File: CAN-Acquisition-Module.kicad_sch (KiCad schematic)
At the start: 0 parts

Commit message: Finished CAN section
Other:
- sheet CANbus ports: added CAN_PIN5, CAN_PIN8; removed none
- sheet MCU ports: added CAN_PIN5, CAN_PIN8; removed none
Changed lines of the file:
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@@
 (kicad_sch (version 20211123) (generator eeschema)
   (paper "A4")
-  (wire (pts (xy 88.9 46.99) (xy 73.66 46.99))
+  (wire (pts (xy 123.19 67.31) (xy 99.06 67.31))
     (stroke (width 0) (type default) (color 0 0 0 0))
   )
@@
     (stroke (width 0) (type default) (color 0 0 0 0))
   )
+  (wire (pts (xy 101.6 69.85) (xy 101.6 107.95))
+    (stroke (width 0) (type default) (color 0 0 0 0))
+  )
   (wire (pts (xy 123.19 60.96) (xy 91.44 60.96))
     (stroke (width 0) (type default) (color 0 0 0 0))
@@
     (stroke (width 0) (type default) (color 0 0 0 0))
   )
+  (wire (pts (xy 99.06 105.41) (xy 73.66 105.41))
+    (stroke (width 0) (type default) (color 0 0 0 0))
+  )
+  (wire (pts (xy 123.19 69.85) (xy 101.6 69.85))
+    (stroke (width 0) (type default) (color 0 0 0 0))
+  )
+  (wire (pts (xy 99.06 67.31) (xy 99.06 105.41))
+    (stroke (width 0) (type default) (color 0 0 0 0))
+  )
   (wire (pts (xy 91.44 60.96) (xy 91.44 99.06))
     (stroke (width 0) (type default) (color 0 0 0 0))
   )
-  (wire (pts (xy 88.9 34.29) (xy 88.9 46.99))
-    (stroke (width 0) (type default) (color 0 0 0 0))
-  )
   (wire (pts (xy 153.67 31.75) (xy 153.67 43.18))
     (stroke (width 0) (type default) (color 0 0 0 0))
   )
-  (wire (pts (xy 43.18 52.07) (xy 39.37 52.07))
+  (wire (pts (xy 41.91 39.37) (xy 39.37 39.37))
+    (stroke (width 0) (type default) (color 0 0 0 0))
+  )
+  (wire (pts (xy 101.6 107.95) (xy 73.66 107.95))
     (stroke (width 0) (type default) (color 0 0 0 0))
   )
@@
     (stroke (width 0) (type default) (color 0 0 0 0))
   )
-  (wire (pts (xy 39.37 52.07) (xy 39.37 101.6))
-    (stroke (width 0) (type default) (color 0 0 0 0))
-  )
-  (wire (pts (xy 140.97 34.29) (xy 88.9 34.29))
+  (wire (pts (xy 39.37 39.37) (xy 39.37 101.6))
+    (stroke (width 0) (type default) (color 0 0 0 0))
+  )
+  (wire (pts (xy 72.39 34.29) (xy 140.97 34.29))
     (stroke (width 0) (type default) (color 0 0 0 0))
   )
@@
       (effects (font (size 1.27 1.27)) (justify right))
     )
-    (pin "CAN_TX" input (at 123.19 60.96 180)
-      (effects (font (size 1.27 1.27)) (justify left))
-    )
     (pin "CAN_RX" input (at 123.19 63.5 180)
       (effects (font (size 1.27 1.27)) (justify left))
     )
-  )
-  (sheet (at 43.18 43.18) (size 30.48 24.13) (fields_autoplaced)
+    (pin "CAN_PIN8" output (at 123.19 67.31 180)
+      (effects (font (size 1.27 1.27)) (justify left))
+    )
+    (pin "CAN_PIN5" output (at 123.19 69.85 180)
+      (effects (font (size 1.27 1.27)) (justify left))
+    )
+    (pin "CAN_TX" output (at 123.19 60.96 180)
+      (effects (font (size 1.27 1.27)) (justify left))
+    )
+  )
+  (sheet (at 41.91 30.48) (size 30.48 24.13) (fields_autoplaced)
     (stroke (width 0) (type solid) (color 0 0 0 0))
     (fill (color 0 0 0 0.0000))
-    (property "Sheet name" "Power" (id 0) (at 43.18 42.4684 0)
+    (property "Sheet name" "Power" (id 0) (at 41.91 29.7684 0)
       (effects (font (size 1.27 1.27)) (justify left bottom))
     )
-    (property "Sheet file" "CAN-Acquisition-Module_Power.kicad_sch" (id 1) (at 43.18 67.8946 0)
+    (property "Sheet file" "CAN-Acquisition-Module_Power.kicad_sch" (id 1) (at 41.91 55.1946 0)
       (effects (font (size 1.27 1.27)) (justify left top))
     )
-    (pin "V_CAN" input (at 43.18 52.07 180)
-      (effects (font (size 1.27 1.27)) (justify left))
-    )
-    (pin "V_USB" input (at 73.66 46.99 0)
+    (pin "V_CAN" input (at 41.91 39.37 180)
+      (effects (font (size 1.27 1.27)) (justify left))
+    )
+    (pin "V_USB" input (at 72.39 34.29 0)
       (effects (font (size 1.27 1.27)) (justify right))
     )
@@
       (effects (font (size 1.27 1.27)) (justify right))
     )
-    (pin "CAN_RX" input (at 73.66 101.6 0)
+    (pin "CAN_PIN8" input (at 73.66 105.41 0)
+      (effects (font (size 1.27 1.27)) (justify right))
+    )
+    (pin "CAN_PIN5" input (at 73.66 107.95 0)
+      (effects (font (size 1.27 1.27)) (justify right))
+    )
+    (pin "CAN_RX" output (at 73.66 101.6 0)
       (effects (font (size 1.27 1.27)) (justify right))
     )
@@
       (reference "#PWR?") (unit 1) (value "GND") (footprint "")
     )
+    (path "/6a23b5b9-2864-4994-bd7a-8563b9182093/14ab098c-cdf6-4c2b-873a-413a652c8ff3"
+      (reference "#PWR?") (unit 1) (value "+3.3V") (footprint "")
+    )
     (path "/00000000-0000-0000-0000-0000628fba98/1a6c513b-8826-4fc6-be8a-b124c5226464"
       (reference "#PWR?") (unit 1) (value "GND") (footprint "")
@@
     )
     (path "/6a23b5b9-2864-4994-bd7a-8563b9182093/2430da88-04ae-4554-86f4-b38352234578"
+      (reference "#PWR?") (unit 1) (value "GND") (footprint "")
+    )
+    (path "/6a23b5b9-2864-4994-bd7a-8563b9182093/2fbbc203-31f8-4993-bf01-97a3d719ff97"
       (reference "#PWR?") (unit 1) (value "GND") (footprint "")
     )
@@
       (reference "#PWR?") (unit 1) (value "GND") (footprint "")
     )
+    (path "/6a23b5b9-2864-4994-bd7a-8563b9182093/be75ac2c-6454-4f5d-8edd-4ad70bd6276d"
+      (reference "#PWR?") (unit 1) (value "GND") (footprint "")
+    )
     (path "/6a23b5b9-2864-4994-bd7a-8563b9182093/d32dccac-ba40-4b97-a43f-d2ceaf85d73f"
       (reference "#PWR?") (unit 1) (value "GND") (footprint "")
@@
       (reference "#PWR?") (unit 1) (value "+3.3V") (footprint "")
     )
+    (path "/6a23b5b9-2864-4994-bd7a-8563b9182093/dda03ce5-e120-46e0-8597-3a35c9a772e6"
+      (reference "#PWR?") (unit 1) (value "+3.3V") (footprint "")
+    )
     (path "/00000000-0000-0000-0000-0000628fba98/ddedcedf-4555-4d19-bad5-e9dd0770639d"
       (reference "#PWR?") (unit 1) (value "GND") (footprint "")
     )
+    (path "/6a23b5b9-2864-4994-bd7a-8563b9182093/e70d5354-397b-4ea4-a225-d4fa715af3bd"
+      (reference "#PWR?") (unit 1) (value "GND") (footprint "")
+    )
     (path "/6a23b5b9-2864-4994-bd7a-8563b9182093/edd17358-9720-40f3-bb9c-b039179ec970"
       (reference "#PWR?") (unit 1) (value "GND") (footprint "")
@@
     )
     (path "/2306ed72-7073-467c-a255-2365c3b83f36/faa4a203-2c3e-4e45-87a6-ff0eb6a4b99f"
+      (reference "#PWR?") (unit 1) (value "GND") (footprint "")
+    )
+    (path "/6a23b5b9-2864-4994-bd7a-8563b9182093/fb2e8c3c-f406-41c1-92ba-9511cdd26a4d"
       (reference "#PWR?") (unit 1) (value "GND") (footprint "")
     )
@@
       (reference "C?") (unit 1) (value "1 uF") (footprint "Capacitor_SMD:C_0603_1608Metric")
     )
+    (path "/6a23b5b9-2864-4994-bd7a-8563b9182093/82a72df0-9101-40a1-a39e-495f466dd76d"
+      (reference "C?") (unit 1) (value "F") (footprint "Capacitor_SMD:C_0603_1608Metric")
+    )
+    (path "/6a23b5b9-2864-4994-bd7a-8563b9182093/9b59bb94-5ec5-41d6-a90a-50c77b045610"
+      (reference "C?") (unit 1) (value "F") (footprint "Capacitor_SMD:C_0603_1608Metric")
+    )
     (path "/6a23b5b9-2864-4994-bd7a-8563b9182093/a57b452e-51f4-4a6f-81d8-6d70dc434fc1"
       (reference "C?") (unit 1) (value "47 pF") (footprint "Capacitor_SMD:C_0603_1608Metric")
@@
       (reference "R?") (unit 1) (value "100 Ω") (footprint "Resistor_SMD:R_0805_2012Metric")
     )
+    (path "/6a23b5b9-2864-4994-bd7a-8563b9182093/0c6df487-3e31-43d7-bd79-da39a42b0f83"
+      (reference "R?") (unit 1) (value "Ω") (footprint "Resistor_SMD:R_0603_1608Metric")
+    )
+    (path "/6a23b5b9-2864-4994-bd7a-8563b9182093/1199abe3-116f-474b-9e98-49648be6ba96"
+      (reference "R?") (unit 1) (value " Ω") (footprint "Resistor_SMD:R_0603_1608Metric")
+    )
+    (path "/6a23b5b9-2864-4994-bd7a-8563b9182093/1cf81b43-2c10-41da-9491-13a80c1363a9"
+      (reference "R?") (unit 1) (value " Ω") (footprint "Resistor_SMD:R_0603_1608Metric")
+    )
     (path "/6a23b5b9-2864-4994-bd7a-8563b9182093/30955db8-291f-483c-8e4c-3c1d0d742d2b"
       (reference "R?") (unit 1) (value "59Ω-62Ω") (footprint "Resistor_SMD:R_1206_3216Metric")
@@
       (reference "R?") (unit 1) (value "27 Ω") (footprint "Resistor_SMD:R_0603_1608Metric")
     )
+    (path "/6a23b5b9-2864-4994-bd7a-8563b9182093/62f65d79-a6a8-40d5-8263-0bce308bb147"
+      (reference "R?") (unit 1) (value "1 kΩ") (footprint "Resistor_SMD:R_0603_1608Metric")
+    )
     (path "/2306ed72-7073-467c-a255-2365c3b83f36/a907d3ec-4367-4ba0-821c-bcd0f98d1cbc"
       (reference "R?") (unit 1) (value "10 kΩ") (footprint "Resistor_SMD:R_0603_1608Metric")
@@
       (reference "R?") (unit 1) (value "47 kΩ") (footprint "Resistor_SMD:R_0603_1608Metric")
     )
+    (path "/6a23b5b9-2864-4994-bd7a-8563b9182093/e90c2505-6430-498e-9243-2604403d18d0"
+      (reference "R?") (unit 1) (value " Ω") (footprint "Resistor_SMD:R_0603_1608Metric")
+    )
     (path "/2306ed72-7073-467c-a255-2365c3b83f36/ec01bf59-6fcb-4ded-ba21-75edfeff7f43"
       (reference "R?") (unit 1) (value "27 Ω") (footprint "Resistor_SMD:R_0603_1608Metric")
     )
+    (path "/6a23b5b9-2864-4994-bd7a-8563b9182093/ef53684a-960f-4291-abcd-f8fe274048cb"
+      (reference "R?") (unit 1) (value "Ω") (footprint "Resistor_SMD:R_0603_1608Metric")
+    )
+    (path "/6a23b5b9-2864-4994-bd7a-8563b9182093/f4e8f079-13e2-474d-b2a5-b77899afb5ca"
+      (reference "R?") (unit 1) (value "22 kΩ") (footprint "Resistor_SMD:R_0603_1608Metric")
+    )
     (path "/6a23b5b9-2864-4994-bd7a-8563b9182093/fcbff347-48de-4a86-b8ce-9f3e8ed81a79"
       (reference "R?") (unit 1) (value "59Ω-62Ω") (footprint "Resistor_SMD:R_1206_3216Metric")
     )
     (path "/00000000-0000-0000-0000-0000628fa103/00000000-0000-0000-0000-0000628f5983"
-      (reference "U?") (unit 1) (value "M483SGCAE2A") (footprint "Package_QFP:LQFP-64_7x7mm_P0.4mm")
+      (reference "U?") (unit 1) (value "M483SGCAE") (footprint "Package_QFP:LQFP-64_7x7mm_P0.4mm")
     )
     (path "/00000000-0000-0000-0000-0000628fba98/00000000-0000-0000-0000-000062a4568c"

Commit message: Added stuff and cleanup
Added LED, Power outputs, additional descriptions
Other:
- added sheet LED (CAN-Acquisition-Module_LED.kicad_sch)
- sheet MCU ports: added FAN_PWM_CTRL, FAN_TACH, LED_B, LED_G, LED_R, POWER_OUT, USB_OTG_ID; removed USB_ID
- sheet Power ports: added FAN_PWM_CTRL, FAN_TACH, POWER_OUTPUT; removed none
- sheet USB ports: added USB_OTG_ID; removed USB_ID

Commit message: Added empty sheets
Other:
- added sheet Analog (CAN_Acquisition_Module_Analog.kicad_sch)
- added sheet Screen (CAN-Acquisition-Module_Screen.kicad_sch)
- added sheet Sensors (CAN-Acqusition-Module_Sensors.kicad_sch)
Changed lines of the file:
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@@
+    )
+  )
+  (sheet (at 212.09 52.07) (size 52.07 35.56) (fields_autoplaced)
+    (stroke (width 0.1524) (type solid) (color 0 0 0 0))
+    (fill (color 0 0 0 0.0000))
+    (property "Sheet name" "Screen" (id 0) (at 212.09 51.3584 0)
+      (effects (font (size 1.27 1.27)) (justify left bottom))
+    )
+    (property "Sheet file" "CAN-Acquisition-Module_Screen.kicad_sch" (id 1) (at 212.09 88.2146 0)
+      (effects (font (size 1.27 1.27)) (justify left top))
+    )
+  )
+  (sheet (at 212.09 106.68) (size 52.07 36.83) (fields_autoplaced)
+    (stroke (width 0.1524) (type solid) (color 0 0 0 0))
+    (fill (color 0 0 0 0.0000))
+    (property "Sheet name" "Sensors" (id 0) (at 212.09 105.9684 0)
+      (effects (font (size 1.27 1.27)) (justify left bottom))
+    )
+    (property "Sheet file" "CAN-Acqusition-Module_Sensors.kicad_sch" (id 1) (at 212.09 144.0946 0)
+      (effects (font (size 1.27 1.27)) (justify left top))
     )
   )
@@
     (pin "CAN_RX" output (at 73.66 101.6 0)
       (effects (font (size 1.27 1.27)) (justify right))
+    )
+  )
+  (sheet (at 123.19 104.14) (size 62.23 40.64) (fields_autoplaced)
+    (stroke (width 0.1524) (type solid) (color 0 0 0 0))
+    (fill (color 0 0 0 0.0000))
+    (property "Sheet name" "Analog" (id 0) (at 123.19 103.4284 0)
+      (effects (font (size 1.27 1.27)) (justify left bottom))
+    )
+    (property "Sheet file" "CAN_Acquisition_Module_Analog.kicad_sch" (id 1) (at 123.19 145.3646 0)
+      (effects (font (size 1.27 1.27)) (justify left top))
     )
   )
@@
     (path "/2306ed72-7073-467c-a255-2365c3b83f36" (page "5"))
     (path "/81a15923-96df-4f0e-bdf1-6a0e43d4751e" (page "6"))
+    (path "/71359799-714b-4644-8db4-495310f76a1b" (page "7"))
+    (path "/5f5345ca-f2d2-466f-a4ac-3c846c4226e8" (page "8"))
+    (path "/341b7c98-b7c0-49e4-b19a-093f835f71de" (page "9"))
   )
   (symbol_instances

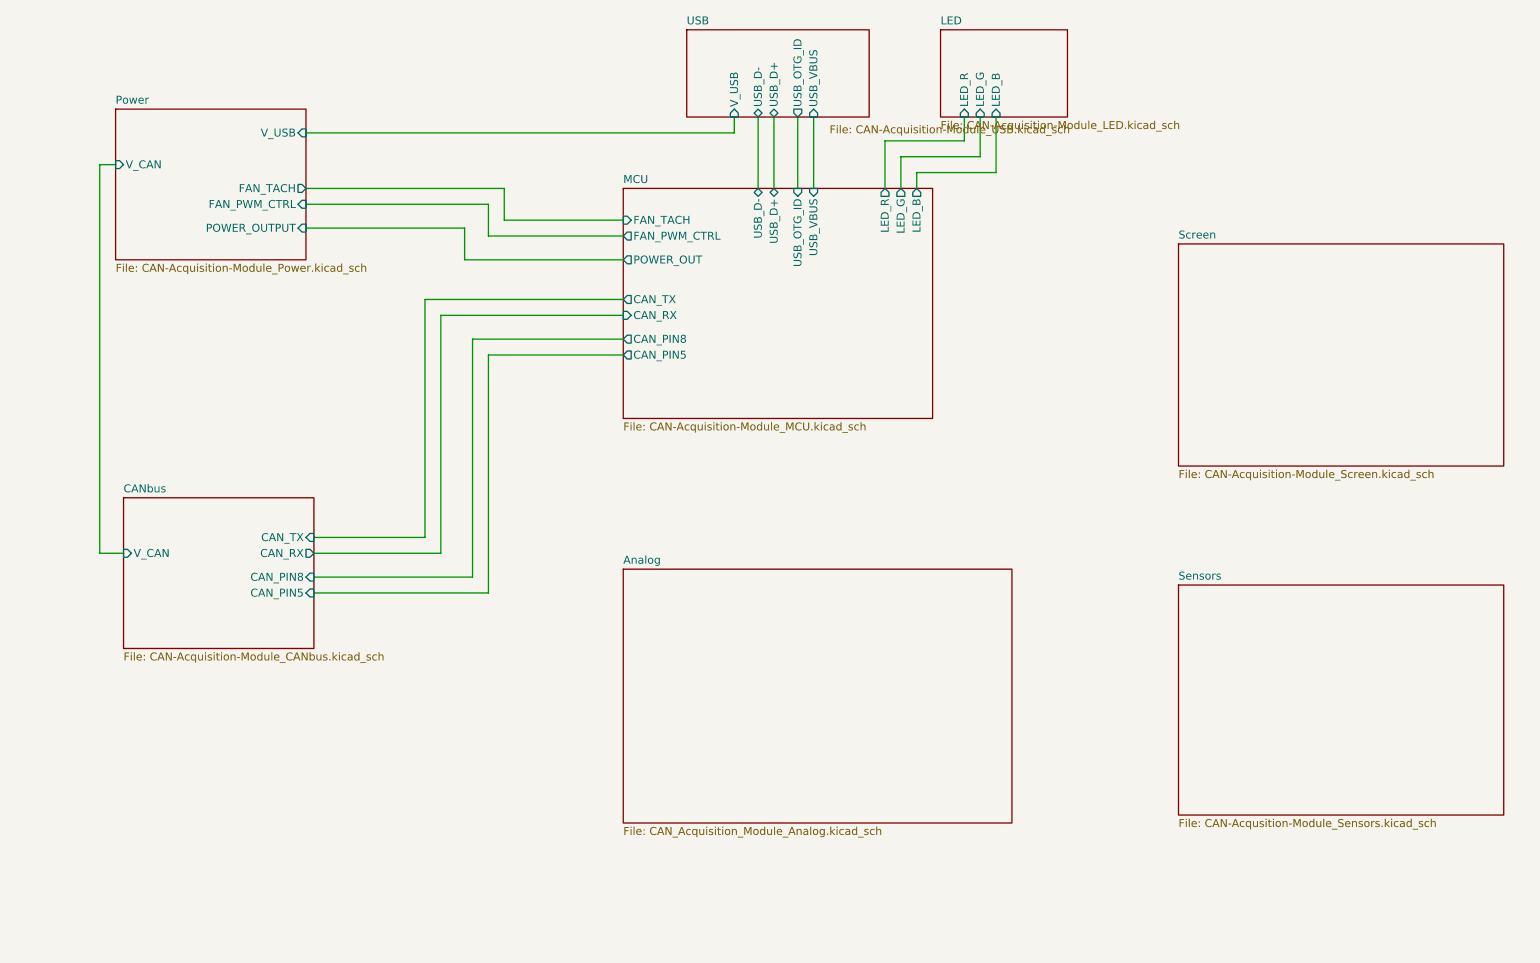
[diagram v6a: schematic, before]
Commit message: Added analog and sensors sections
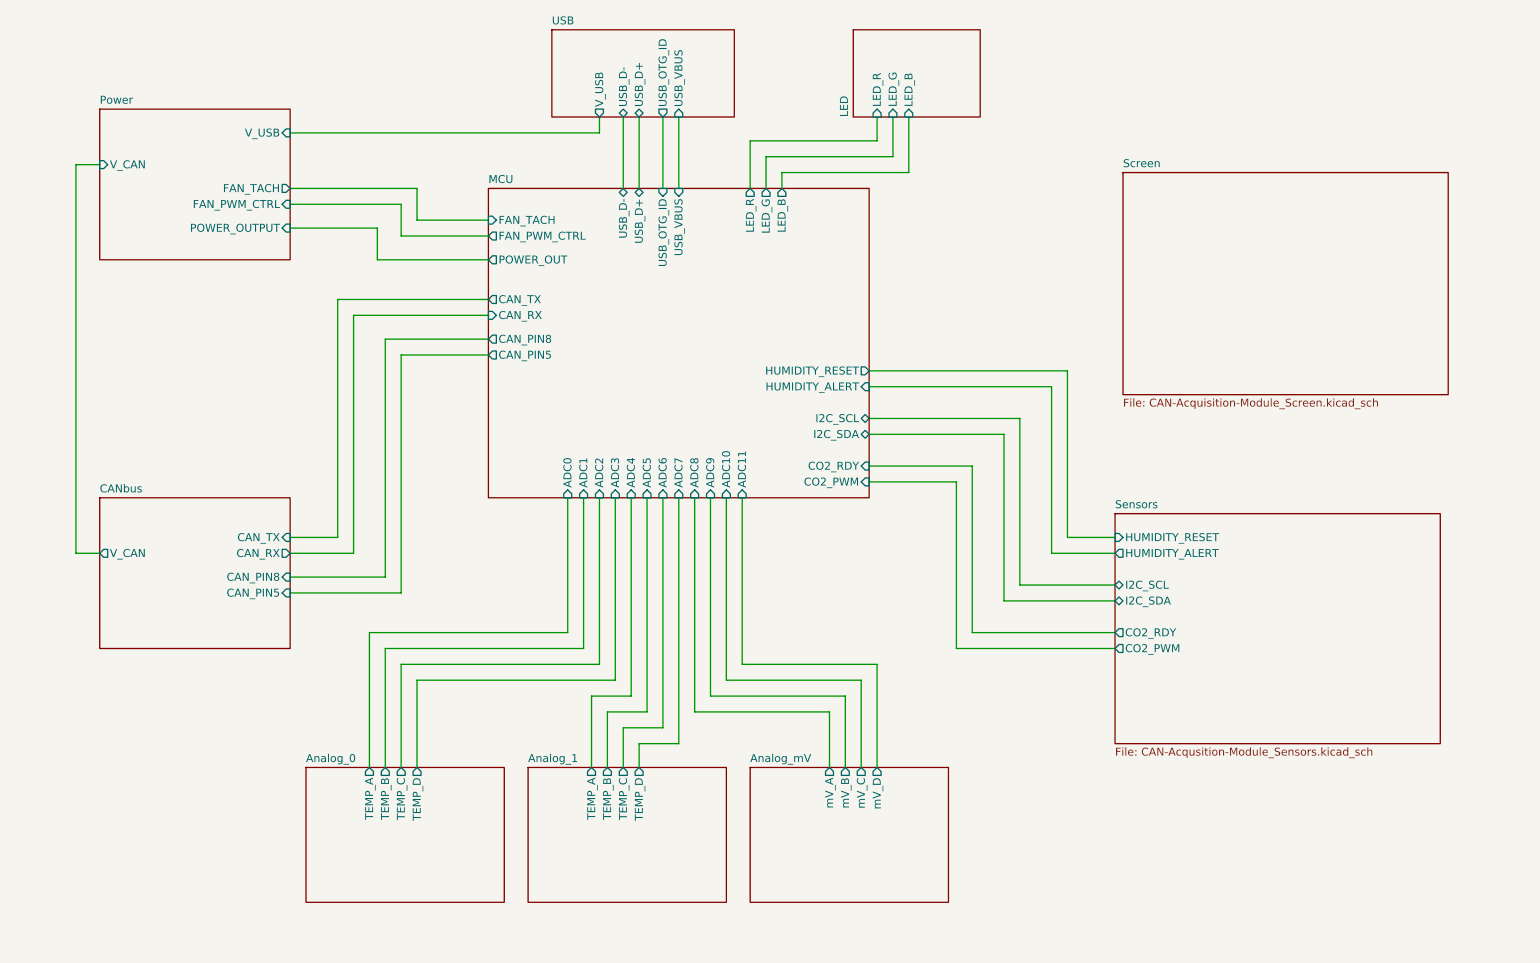
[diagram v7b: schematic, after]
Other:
- sheet Analog renamed Analog_0
- added sheet Analog_1 (CAN-Acquisition-Module_Analog_0.kicad_sch)
- added sheet Analog_mV (CAN-Acquisition-Module_Analog_mV.kicad_sch)
- sheet Analog_0: file CAN_Acquisition_Module_Analog.kicad_sch -> CAN-Acquisition-Module_Analog_0.kicad_sch
- sheet Analog_0 ports: added TEMP_A, TEMP_B, TEMP_C, TEMP_D; removed none
- sheet MCU ports: added ADC0, ADC1, ADC10, ADC11, ADC2, ADC3, ADC4, ADC5, ADC6, ADC7, ADC8, ADC9, CO2_PWM, CO2_RDY, HUMIDITY_ALERT, HUMIDITY_RESET, I2C_SCL, I2C_SDA; removed none
- sheet Sensors ports: added CO2_PWM, CO2_RDY, HUMIDITY_ALERT, HUMIDITY_RESET, I2C_SCL, I2C_SDA; removed none
- company: (none) -> École de Technologie Supérieure - Laboratoire thermique et science du bâtiment (LTSB)
- title: (none) -> CANbus Acquisition Module

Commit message: Added screen sections and annotations
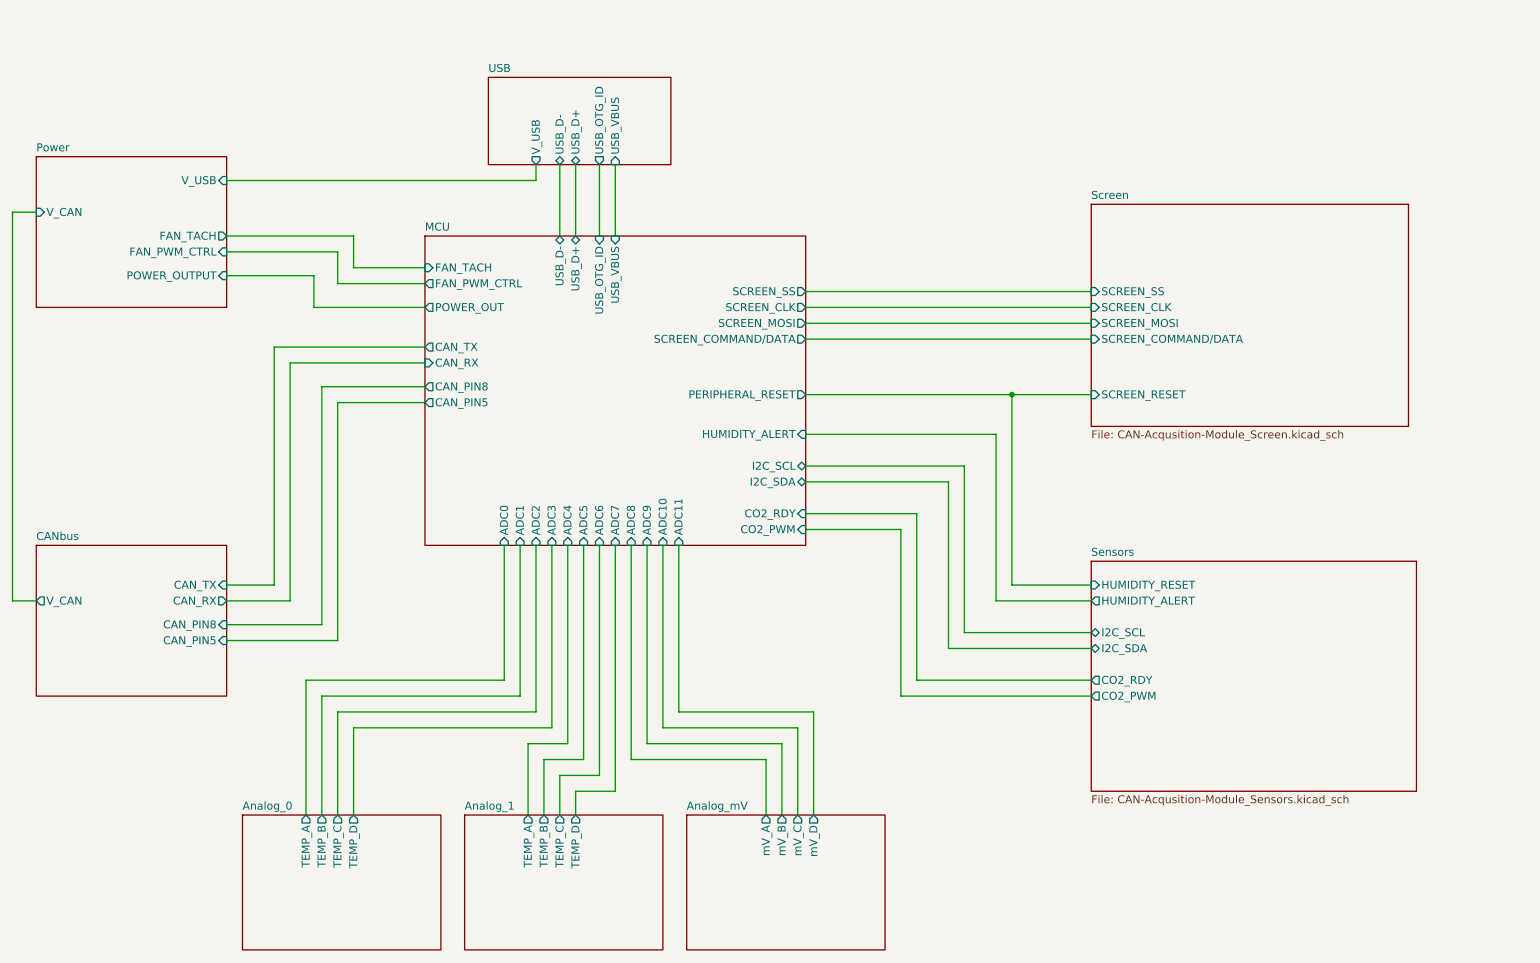
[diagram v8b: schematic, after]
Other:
- removed sheet LED
- sheet MCU ports: added PERIPHERAL_RESET, SCREEN_CLK, SCREEN_COMMAND/DATA, SCREEN_MOSI, SCREEN_SS; removed HUMIDITY_RESET, LED_B, LED_G, LED_R
- sheet Screen: file CAN-Acquisition-Module_Screen.kicad_sch -> CAN-Acqusition-Module_Screen.kicad_sch
- sheet Screen ports: added SCREEN_CLK, SCREEN_COMMAND/DATA, SCREEN_MOSI, SCREEN_RESET, SCREEN_SS; removed none
